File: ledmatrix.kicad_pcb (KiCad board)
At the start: 2 copper layers, 75.6 x 37.8 mm, 32 parts, among them J1 BUS_IN1, J2 BUS_IN2, J3 BUS_OUT1, J4 BUS_OUT2, Q1 PMV50XP, Q2 PMV50XP, Q3 PMV50XP, Q4 PMV50XP, Q5 PMV50XP, Q6 PMV50XP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

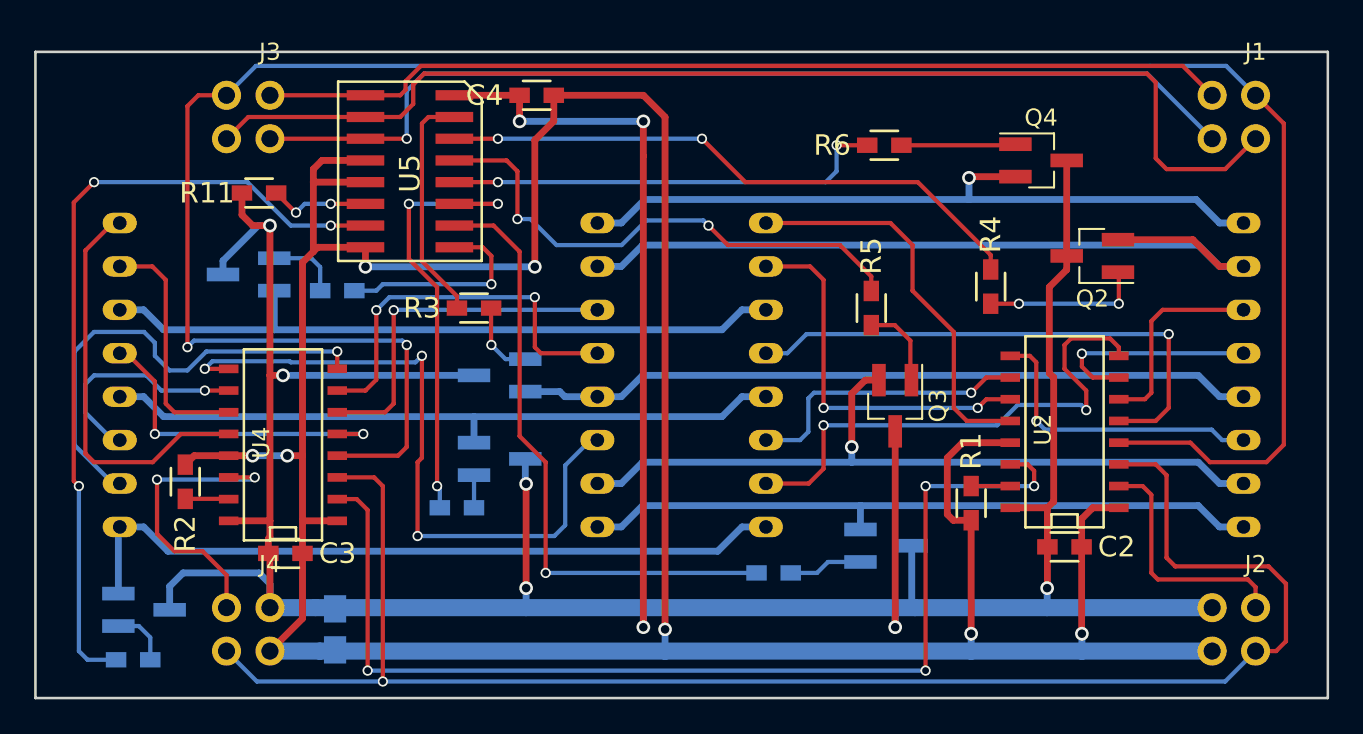
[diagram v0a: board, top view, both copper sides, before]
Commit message: adjust silkscreen
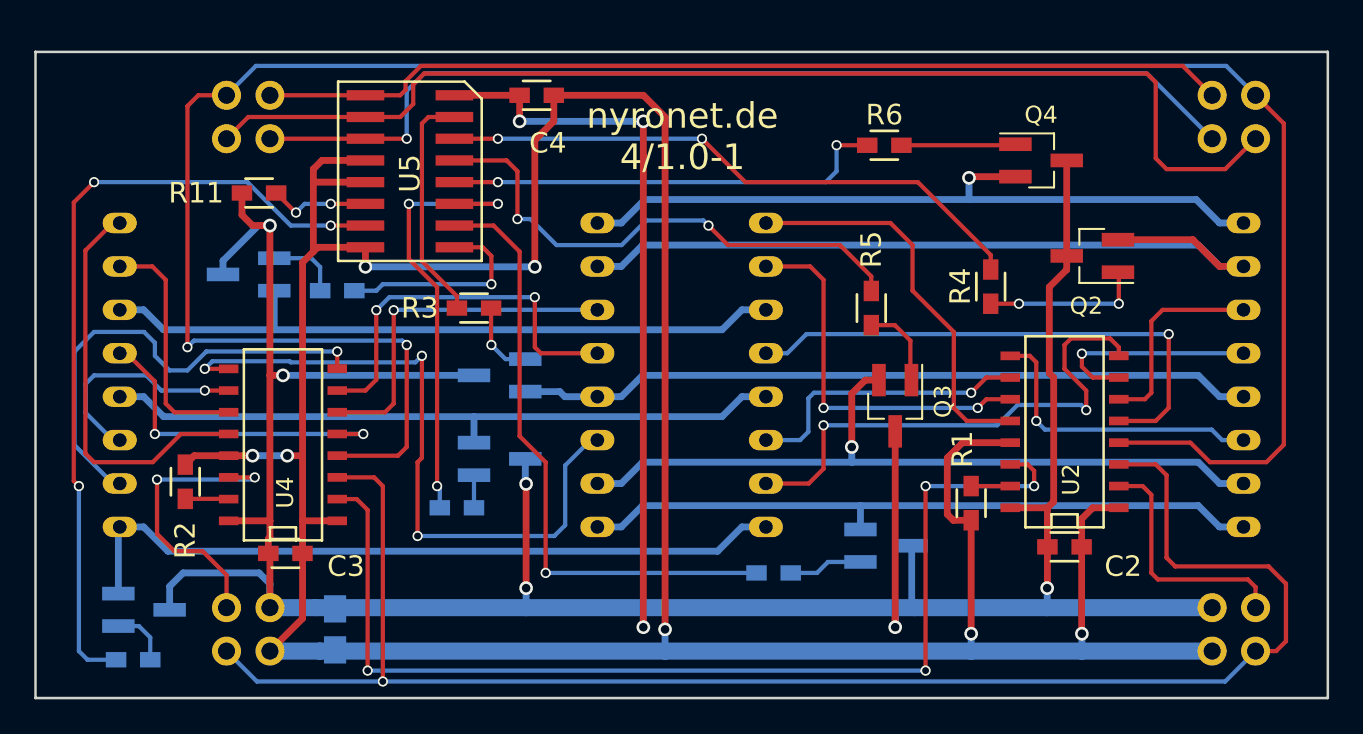
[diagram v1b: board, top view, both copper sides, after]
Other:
- board text added: "nyronet.de 4/1.0-1"
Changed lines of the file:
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@@
     (area 25.024999 24.325 106.999001 64.675)
     (thickness 1.6)
-    (drawings 4)
+    (drawings 5)
     (tracks 545)
     (zones 0)
@@
   (module footprints:0603_HAND (layer F.Cu)
     (at 51.054 40.386 180)
-    (fp_text reference R3 (at 3.048 0 180) (layer F.SilkS)
+    (fp_text reference R3 (at 3.175 0 180) (layer F.SilkS)
       (effects (font (size 1.2 1.2) (thickness 0.2)))
     )
@@
     (tags SOT-23)
     (attr smd)
-    (fp_text reference Q2 (at 0 -2.5 180) (layer F.SilkS)
+    (fp_text reference Q2 (at 0.357 -2.921 180) (layer F.SilkS)
       (effects (font (size 1 1) (thickness 0.15)))
     )
@@
     (tags SOT-23)
     (attr smd)
-    (fp_text reference Q3 (at 0 -2.5 270) (layer F.SilkS)
+    (fp_text reference Q3 (at -0.254 -2.794 270) (layer F.SilkS)
       (effects (font (size 1 1) (thickness 0.15)))
     )
@@
     (tags SOT-23)
     (attr smd)
-    (fp_text reference Q4 (at 0 -2.5) (layer F.SilkS)
+    (fp_text reference Q4 (at 0 -2.667) (layer F.SilkS)
       (effects (font (size 1 1) (thickness 0.15)))
     )
@@
     (tags SOT-23)
     (attr smd)
-    (fp_text reference Q5 (at 0 2.5) (layer B.SilkS)
+    (fp_text reference Q5 (at 0.913 3.114) (layer B.SilkS)
       (effects (font (size 1 1) (thickness 0.15)) (justify mirror))
     )
@@
     (tags SOT-23)
     (attr smd)
-    (fp_text reference Q6 (at 0 2.5) (layer B.SilkS)
+    (fp_text reference Q6 (at -0.103 2.733) (layer B.SilkS)
       (effects (font (size 1 1) (thickness 0.15)) (justify mirror))
     )
@@
     (tags SOT-23)
     (attr smd)
-    (fp_text reference Q7 (at 0 2.5 180) (layer B.SilkS)
+    (fp_text reference Q7 (at 0.024 -2.601 180) (layer B.SilkS)
       (effects (font (size 1 1) (thickness 0.15)) (justify mirror))
     )
@@
     (tags SOT-23)
     (attr smd)
-    (fp_text reference Q8 (at 0 2.5) (layer B.SilkS)
+    (fp_text reference Q8 (at 0 -2.667) (layer B.SilkS)
       (effects (font (size 1 1) (thickness 0.15)) (justify mirror))
     )
@@
   (module footprints:0603_HAND (layer F.Cu)
     (at 80.137 51.8 90)
-    (fp_text reference R1 (at 3.048 0 90) (layer F.SilkS)
+    (fp_text reference R1 (at 3.159 -0.508 90) (layer F.SilkS)
       (effects (font (size 1.2 1.2) (thickness 0.2)))
     )
@@
   (module footprints:0603_HAND (layer F.Cu)
     (at 34.163 50.546 270)
-    (fp_text reference R2 (at 3.048 0 270) (layer F.SilkS)
+    (fp_text reference R2 (at 3.429 0 270) (layer F.SilkS)
       (effects (font (size 1.2 1.2) (thickness 0.2)))
     )
@@
   (module footprints:0603_HAND (layer F.Cu)
     (at 81.28 39.132 90)
-    (fp_text reference R4 (at 3.048 0 90) (layer F.SilkS)
+    (fp_text reference R4 (at 0.016 -1.778 90) (layer F.SilkS)
       (effects (font (size 1.2 1.2) (thickness 0.2)))
     )
@@
   (module footprints:0603_HAND (layer F.Cu)
     (at 74.295 40.386 90)
-    (fp_text reference R5 (at 3.048 0 90) (layer F.SilkS)
+    (fp_text reference R5 (at 3.429 0 90) (layer F.SilkS)
       (effects (font (size 1.2 1.2) (thickness 0.2)))
     )
@@
   (module footprints:0603_HAND (layer F.Cu)
     (at 75.057 30.861 180)
-    (fp_text reference R6 (at 3.048 0 180) (layer F.SilkS)
+    (fp_text reference R6 (at 0 1.778 180) (layer F.SilkS)
       (effects (font (size 1.2 1.2) (thickness 0.2)))
     )
@@
   (module footprints:0603_HAND (layer B.Cu)
     (at 50.054 52.07 180)
-    (fp_text reference R7 (at 3.048 0 180) (layer B.SilkS)
+    (fp_text reference R7 (at 3.318 -0.254 180) (layer B.SilkS)
       (effects (font (size 1.2 1.2) (thickness 0.2)) (justify mirror))
     )
@@
   (module footprints:0603_HAND (layer B.Cu)
     (at 68.58 55.88 180)
-    (fp_text reference R8 (at 3.048 0 180) (layer B.SilkS)
+    (fp_text reference R8 (at 3.429 -0.508 180) (layer B.SilkS)
       (effects (font (size 1.2 1.2) (thickness 0.2)) (justify mirror))
     )
@@
   (module footprints:0603_HAND (layer B.Cu)
     (at 43.053 39.37)
-    (fp_text reference R9 (at 3.048 0) (layer B.SilkS)
+    (fp_text reference R9 (at 3.429 0) (layer B.SilkS)
       (effects (font (size 1.2 1.2) (thickness 0.2)) (justify mirror))
     )
@@
   (module footprints:0603_HAND (layer B.Cu)
     (at 31.115 60.96 180)
-    (fp_text reference R10 (at 3.048 0 180) (layer B.SilkS)
+    (fp_text reference R10 (at 3.175 1.016 270) (layer B.SilkS)
       (effects (font (size 1.2 1.2) (thickness 0.2)) (justify mirror))
     )
@@
   (module footprints:LEDMATRIX_1588BS locked (layer B.Cu)
     (at 82.1 44.3 270)
-    (fp_text reference U1 (at -10 0 540) (layer B.SilkS)
+    (fp_text reference U1 (at -10 0 360) (layer B.SilkS) hide
       (effects (font (size 1.2 1.2) (thickness 0.15)) (justify mirror))
     )
@@
     (tags "CMS SOJ")
     (attr smd)
-    (fp_text reference U2 (at 0.127 -1.27 90) (layer F.SilkS)
+    (fp_text reference U2 (at -2.794 0.381 90) (layer F.SilkS)
       (effects (font (size 1 1) (thickness 0.15)))
     )
@@
   (module footprints:LEDMATRIX_1588BS locked (layer B.Cu)
     (at 44.3 44.3 270)
-    (fp_text reference U3 (at -10 0 540) (layer B.SilkS)
+    (fp_text reference U3 (at -10 0 360) (layer B.SilkS) hide
       (effects (font (size 1.2 1.2) (thickness 0.15)) (justify mirror))
     )
@@
     (tags "CMS SOJ")
     (attr smd)
-    (fp_text reference U4 (at 0.127 -1.27 90) (layer F.SilkS)
+    (fp_text reference U4 (at -2.794 0.127 90) (layer F.SilkS)
       (effects (font (size 1 1) (thickness 0.15)))
     )
@@
     (descr "Through hole pin header")
     (tags "pin header")
-    (fp_text reference J3 (at 0 -2.54) (layer F.SilkS)
+    (fp_text reference J3 (at 0 -2.54) (layer F.SilkS) hide
       (effects (font (size 1 1) (thickness 0.15)))
     )
@@
     (descr "Through hole pin header")
     (tags "pin header")
-    (fp_text reference J4 (at 0 -2.54) (layer F.SilkS)
+    (fp_text reference J4 (at 0 -2.54) (layer F.SilkS) hide
       (effects (font (size 1 1) (thickness 0.15)))
     )
@@
     (descr "Through hole pin header")
     (tags "pin header")
-    (fp_text reference J2 (at 0 -2.54) (layer F.SilkS)
+    (fp_text reference J2 (at 0 -2.54) (layer F.SilkS) hide
       (effects (font (size 1 1) (thickness 0.15)))
     )
@@
     (descr "Through hole pin header")
     (tags "pin header")
-    (fp_text reference J1 (at 0 -2.54) (layer F.SilkS)
+    (fp_text reference J1 (at 0 -2.54) (layer F.SilkS) hide
       (effects (font (size 1 1) (thickness 0.15)))
     )
@@
     (tags SOT-23)
     (attr smd)
-    (fp_text reference Q1 (at 0 2.5 180) (layer B.SilkS)
+    (fp_text reference Q1 (at -1.929 2.54 180) (layer B.SilkS)
       (effects (font (size 1 1) (thickness 0.15)) (justify mirror))
     )
@@
   (module footprints:0603_HAND (layer F.Cu)
     (at 38.481 33.655 180)
-    (fp_text reference R11 (at 3.048 0 180) (layer F.SilkS)
+    (fp_text reference R11 (at 3.683 0 180) (layer F.SilkS)
       (effects (font (size 1.2 1.2) (thickness 0.2)))
     )
@@
   (module footprints:0805_HAND (layer B.Cu)
     (at 42.926 59.182 270)
-    (fp_text reference C1 (at 0 1.905 270) (layer B.SilkS)
+    (fp_text reference C1 (at 0 -2.159 270) (layer B.SilkS)
       (effects (font (size 1 1) (thickness 0.16)) (justify mirror))
     )
@@
   (module footprints:0603_HAND (layer F.Cu)
     (at 85.598 54.356)
-    (fp_text reference C2 (at 3.048 0) (layer F.SilkS)
+    (fp_text reference C2 (at 3.429 1.143) (layer F.SilkS)
       (effects (font (size 1.2 1.2) (thickness 0.2)))
     )
@@
   (module footprints:0603_HAND (layer F.Cu)
     (at 40.021 54.737)
-    (fp_text reference C3 (at 3.048 0) (layer F.SilkS)
+    (fp_text reference C3 (at 3.54 0.762) (layer F.SilkS)
       (effects (font (size 1.2 1.2) (thickness 0.2)))
     )
@@
   (module footprints:0603_HAND (layer F.Cu)
     (at 54.721 27.94 180)
-    (fp_text reference C4 (at 3.048 0 180) (layer F.SilkS)
+    (fp_text reference C4 (at -0.651 -2.794 180) (layer F.SilkS)
       (effects (font (size 1.2 1.2) (thickness 0.2)))
     )
@@
       (net 1 /VCC))
   )
+  (gr_text "nyronet.de\n4/1.0-1" (at 63.246 30.353 360) (layer F.SilkS)
+    (effects (font (size 1.5 1.5) (thickness 0.3)))
+  )
   (gr_line (start 25.4 25.4) (end 25.4 63.2) (layer Edge.Cuts) (width 0.15))
